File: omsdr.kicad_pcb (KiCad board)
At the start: 2 copper layers, 50 x 50 mm, 58 parts, among them J1 I/Q Out, J2 ANT, J3 ISP, J4 LO, J5 I/Q Out, J8 PWR, SW1 SW_SPST, SW2 SW_SPST, T1 CX2074NL, U1 LT6231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

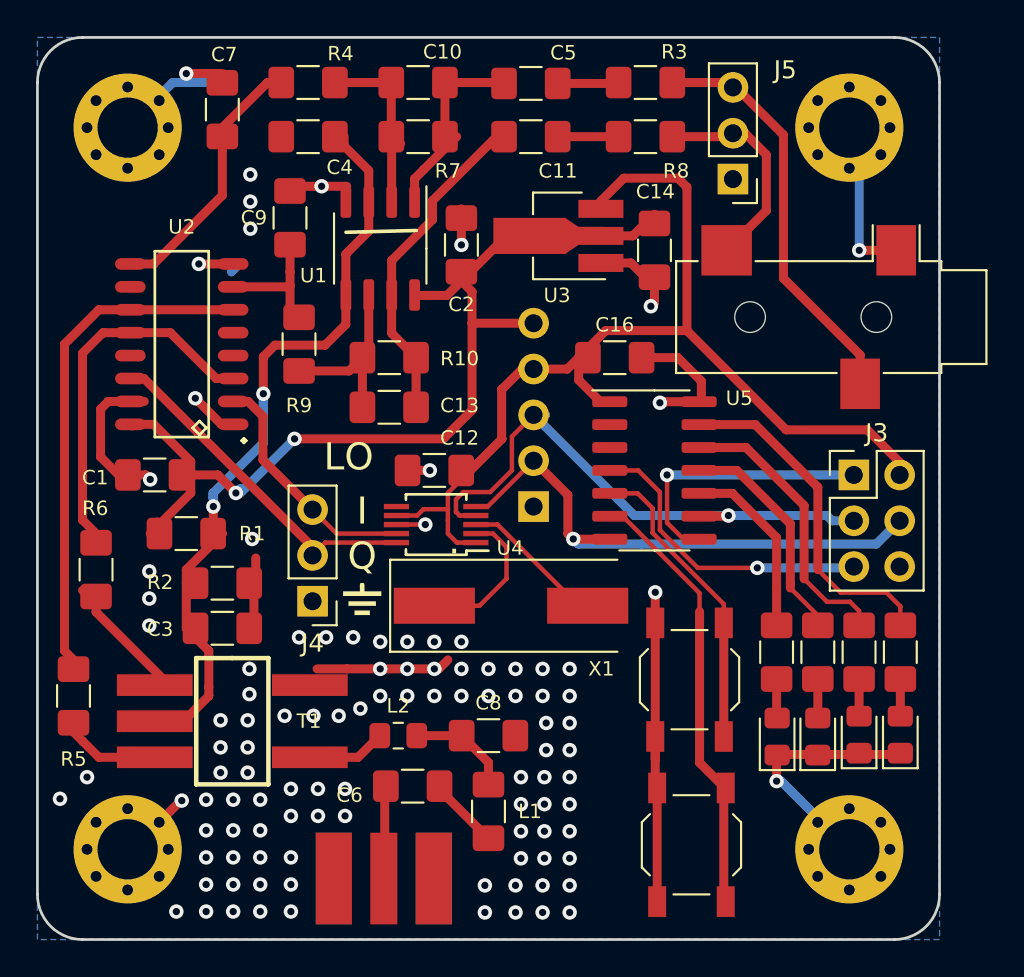
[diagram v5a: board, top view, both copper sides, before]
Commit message: Using FST3253 from the KiCad library (sch & pcb)
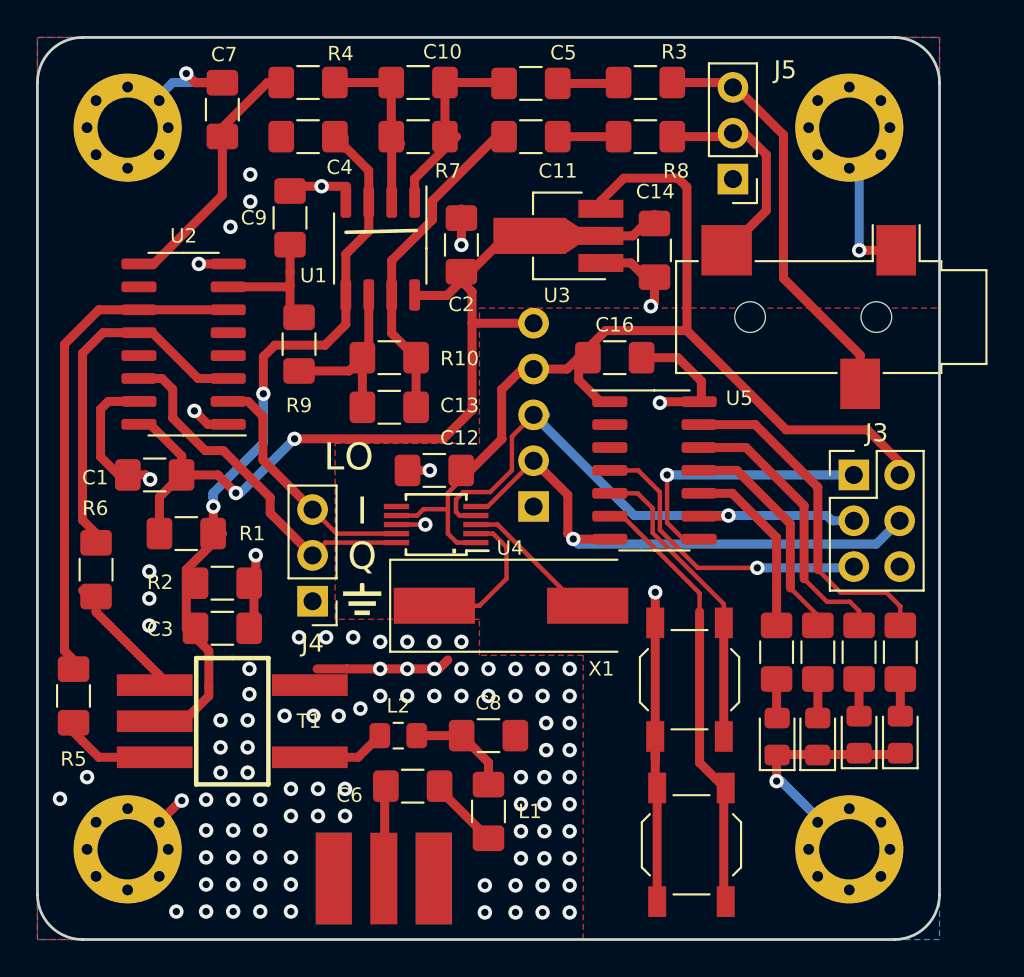
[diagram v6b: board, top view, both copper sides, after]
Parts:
- U2: footprint IPC7351-Most:SOIC127P600X180-16 -> Package_SO:SOIC-16_3.9x9.9mm_P1.27mm
- moved U2 0.10 mm to (108.1, 67.0)
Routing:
- net +5V: track 60.1 -> 58.4 mm
- net Net-(J4-Pad2): track 19.4 -> 20.5 mm
- net GND: track 98.7 -> 97.9 mm
- net Net-(R6-Pad1): track 20.2 -> 19.4 mm
- added copper zone on F.Cu, net GND

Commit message: Replacing some passives with current kicad symbols/footprints
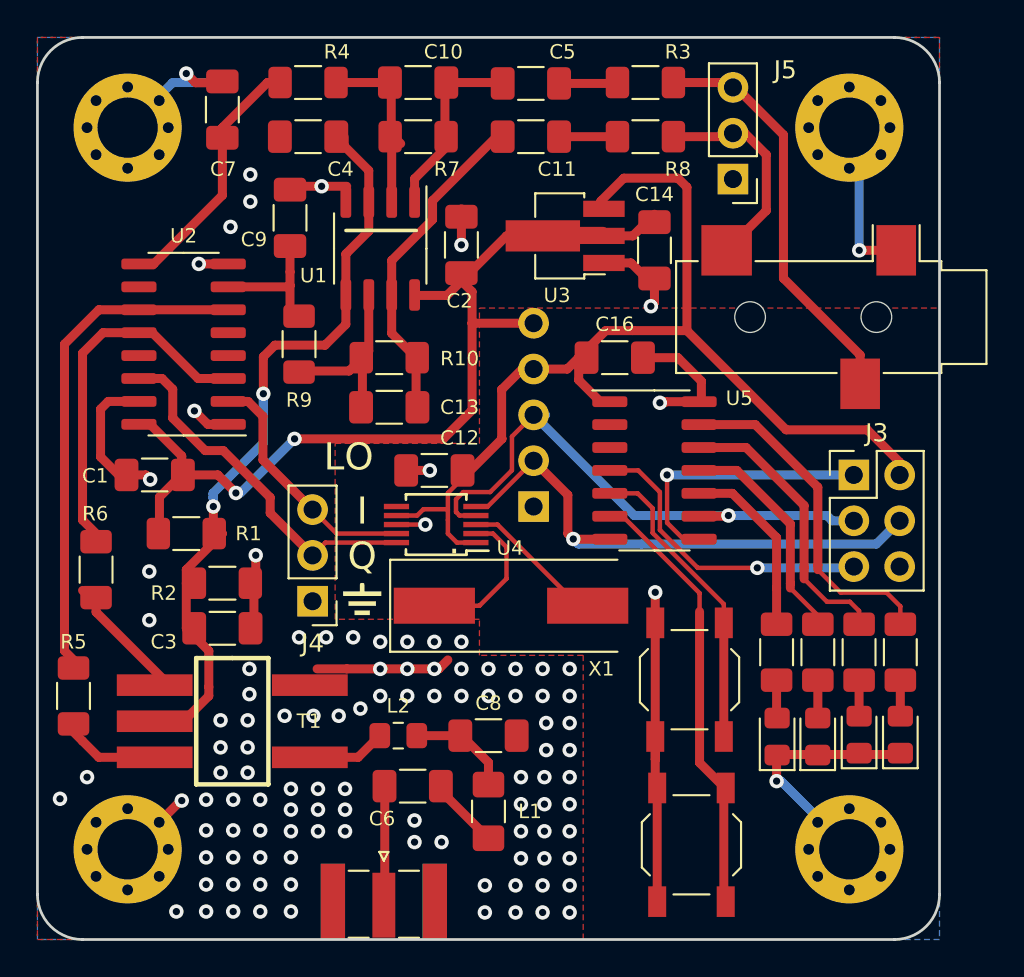
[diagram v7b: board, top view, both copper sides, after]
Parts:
- C1, C10, C11, C12, C13, C14, C16, C2, C3, C4, C5, C6, C7, C8, C9: footprint Capacitor_SMD:C_1206_3216Metric_Pad1.42x1.75mm_HandSolder -> Capacitor_SMD:C_1206_3216Metric_Pad1.33x1.80mm_HandSolder
- J2: footprint local:SMA_edge_mount_small -> Connector_Coaxial:SMA_Samtec_SMA-J-P-X-ST-EM1_EdgeMount
- J8: value PWR -> IO
- R1, R10, R11, R12, R13, R14, R2, R3, R4, R5, R6, R7, R8, R9: footprint Resistor_SMD:R_1206_3216Metric_Pad1.42x1.75mm_HandSolder -> Resistor_SMD:R_1206_3216Metric_Pad1.30x1.75mm_HandSolder
- moved J2 3.00 mm to (119.2, 97.9), turned to 0 degrees
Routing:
- net GND: vias 107 -> 112

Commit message: Using M3 mouting holes from the KiCad library (sch & pcb)
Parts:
- MH1, MH2, MH3, MH4: footprint mech:PTH-3MM-PLUS-SUPPORTED -> MountingHole:MountingHole_3.2mm_M3_Pad_Via
